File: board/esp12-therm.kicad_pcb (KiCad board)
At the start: 2 copper layers, 35.8 x 27.7 mm, 25 parts, among them J1 BATT, J2 I2C, J4 1W, Q1 PMF170XP, U1 TP4056_board, U2 ESP-12E, U3 TLV75533PDBV

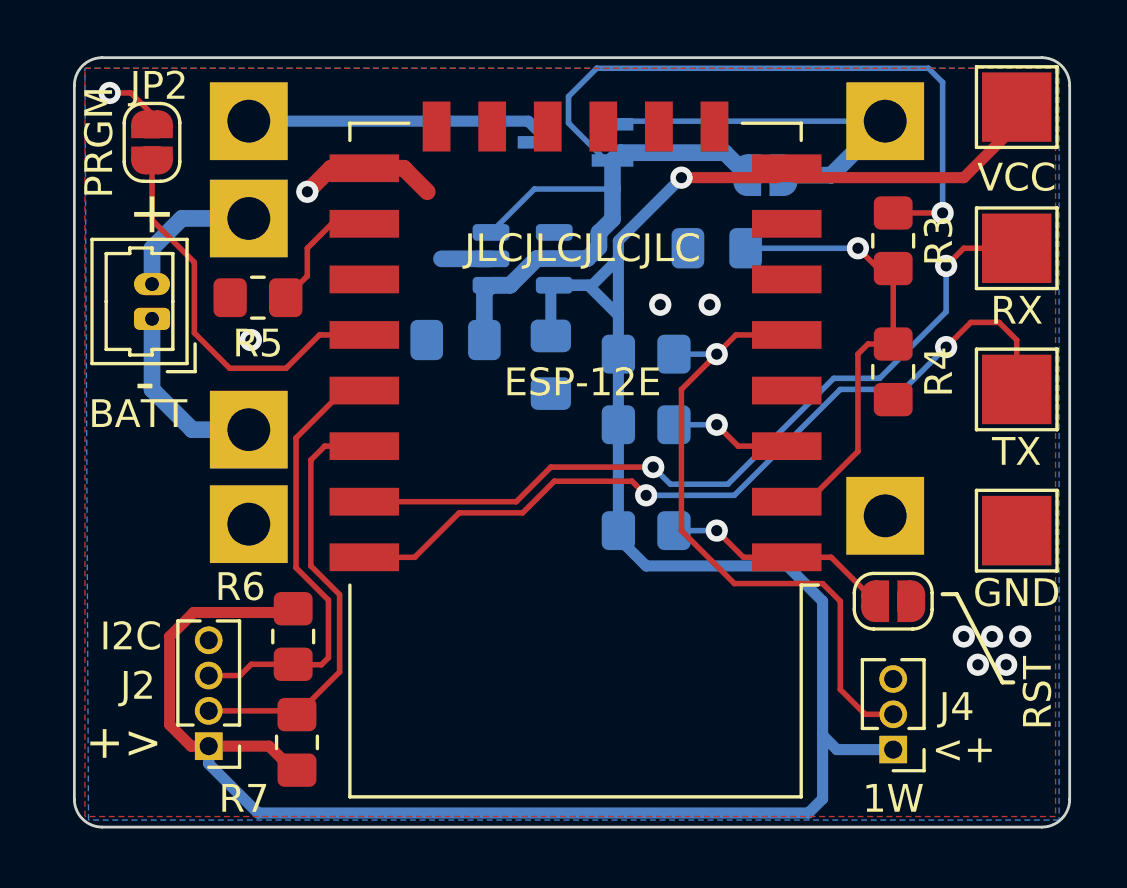
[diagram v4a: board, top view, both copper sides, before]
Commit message: Redesign to make it a fully breakout board: * Add pads for all pins * shrink board ad far as possible * place pull up resistors close to each other at the back * replace nmos with a schottky diode
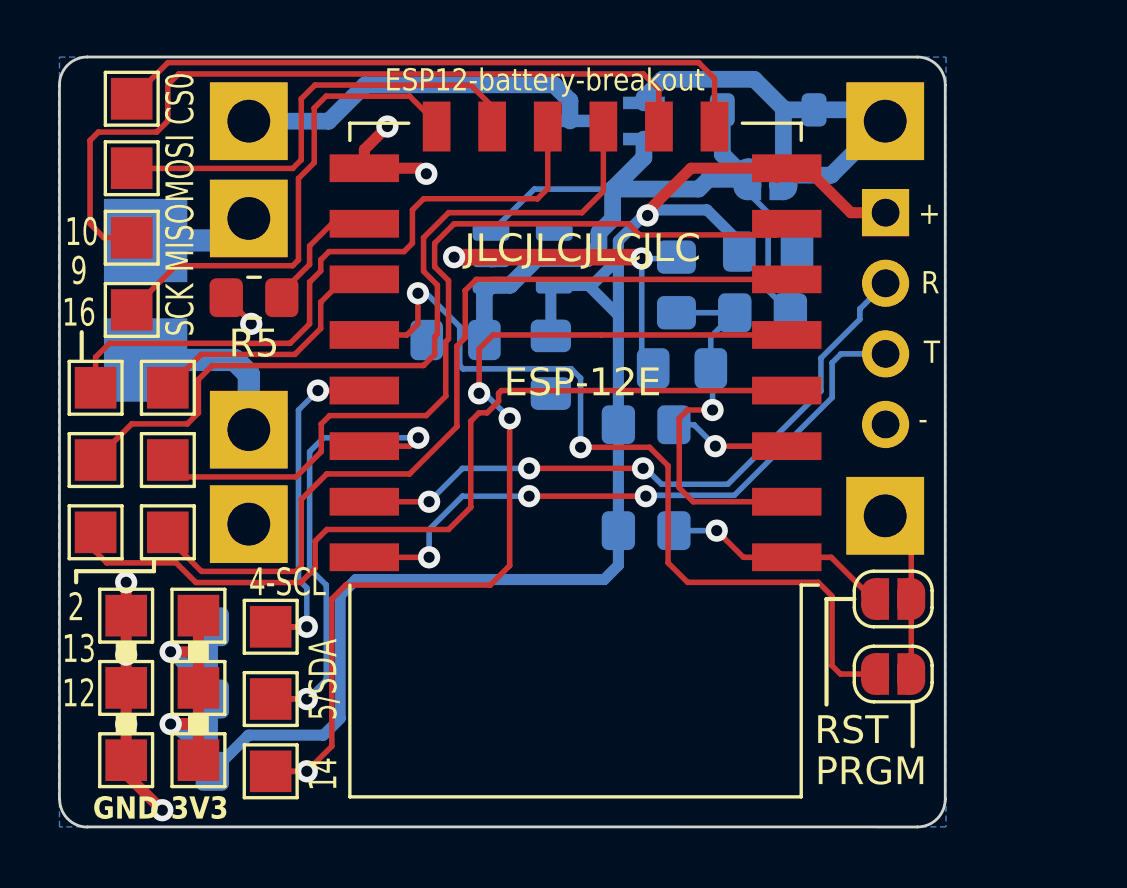
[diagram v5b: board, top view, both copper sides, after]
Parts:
- removed J4: 1W, Connector_PinHeader_1.27mm:PinHeader_1x03_P1.27mm_Vertical
- added C4: 100n, Capacitor_SMD:C_0805_2012Metric_Pad1.18x1.45mm_HandSolder, B.Cu at (122.5, 56.0)
- added D1: LL5817, Diode_SMD:D_SOD-123, B.Cu at (122.5, 50.9)
- added J3: DEBUG, Connector_PinSocket_2.54mm:PinSocket_1x04_P2.54mm_Vertical, F.Cu at (126.7, 54.6)
- added TP10: 10, TestPoint:TestPoint_Pad_1.5x1.5mm, F.Cu at (98.3, 60.9)
- added TP11: 4-SCL, TestPoint:TestPoint_Pad_1.5x1.5mm, F.Cu at (104.6, 69.5)
- added TP12: 2, TestPoint:TestPoint_Pad_1.5x1.5mm, F.Cu at (100.9, 60.9)
- added TP13: 3V3, TestPoint:TestPoint_Pad_1.5x1.5mm, F.Cu at (102.0, 71.7)
- added TP14: 3V3, TestPoint:TestPoint_Pad_1.5x1.5mm, F.Cu at (102.0, 74.3)
- added TP15: 3V3, TestPoint:TestPoint_Pad_1.5x1.5mm, F.Cu at (102.0, 69.1)
- added TP16: GND, TestPoint:TestPoint_Pad_1.5x1.5mm, F.Cu at (99.4, 69.1)
- added TP17: GND, TestPoint:TestPoint_Pad_1.5x1.5mm, F.Cu at (99.4, 74.3)
- added TP18: GND, TestPoint:TestPoint_Pad_1.5x1.5mm, F.Cu at (99.4, 71.7)
- added TP19: 14, TestPoint:TestPoint_Pad_1.5x1.5mm, F.Cu at (104.6, 74.7)
- added TP5: MISO, TestPoint:TestPoint_Pad_1.5x1.5mm, F.Cu at (99.6, 55.5)
- added TP6: MOSI, TestPoint:TestPoint_Pad_1.5x1.5mm, F.Cu at (99.6, 53.0)
- added TP7: SCK, TestPoint:TestPoint_Pad_1.5x1.5mm, F.Cu at (99.6, 58.1)
- added TP8: CS0, TestPoint:TestPoint_Pad_1.5x1.5mm, F.Cu at (99.6, 50.5)
- added TP9: 9, TestPoint:TestPoint_Pad_1.5x1.5mm, F.Cu at (98.3, 63.5)
- J1: value BATT -> B-; footprint Connector_Molex:Molex_PicoBlade_53047-0210_1x02_P1.25mm_Vertical -> TestPoint:TestPoint_Pad_3.0x3.0mm; moved to B.Cu
- J2: value I2C -> B+; footprint Connector_PinHeader_1.27mm:PinHeader_1x04_P1.27mm_Vertical -> TestPoint:TestPoint_Pad_3.0x3.0mm; moved to B.Cu
- R3, R6, R7: moved to B.Cu
- R4: value 470k -> 220k; moved to B.Cu
- TP1: value VCC -> 16; footprint TestPoint:TestPoint_Pad_2.5x2.5mm -> TestPoint:TestPoint_Pad_1.5x1.5mm
- TP2: value RX -> 13; footprint TestPoint:TestPoint_Pad_2.5x2.5mm -> TestPoint:TestPoint_Pad_1.5x1.5mm
- TP3: value TX -> 12; footprint TestPoint:TestPoint_Pad_2.5x2.5mm -> TestPoint:TestPoint_Pad_1.5x1.5mm
- TP4: value GND -> 5/SDA; footprint TestPoint:TestPoint_Pad_2.5x2.5mm -> TestPoint:TestPoint_Pad_1.5x1.5mm
- moved TP1 36.5 mm to (98.3, 66.1), turned to 0 degrees
- moved JP2 32.8 mm to (127.0, 71.2), turned to 180 degrees
- moved TP2 31.5 mm to (100.9, 63.5)
- moved TP3 31.0 mm to (100.9, 66.1)
- moved TP4 27.5 mm to (104.6, 72.1)
- moved R8 20.9 mm to (103.5, 74.7)
- moved J2 18.3 mm to (100.1, 55.6)
- moved R4 8.40 mm to (119.2, 57.2), turned to 90 degrees
- moved R3 5.37 mm to (122.3, 58.2), turned to 180 degrees
- moved C1 4.50 mm to (119.4, 60.2)
- moved R7 2.57 mm to (103.5, 72.1), turned to 0 degrees
- moved R6 1.94 mm to (103.5, 69.5), turned to 0 degrees
- moved J1 1.50 mm to (100.1, 59.9), turned to 180 degrees
- moved Q1 1.37 mm to (116.7, 51.3)
- moved JP3 0.15 mm to (122.4, 53.4)
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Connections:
- C3 pad 1: VCC -> +3V3
- J2 pad 1: VCC -> Net-(J2-Pin_1)
- R1 pad 1: VCC -> +3V3
- R2 pad 1: VCC -> +3V3
- R6 pad 1: VCC -> +3V3
- R7 pad 1: VCC -> +3V3
- R8 pad 1: VCC -> +3V3
- TP1 pad 1: VCC -> Net-(U2-GPIO16)
- TP2 pad 1: RXD -> Net-(U2-GPIO13)
- TP3 pad 1: TXD -> Net-(U2-GPIO12)
- TP4 pad 1: GND -> SDA
- U1 pad 5: Net-(J1-Pin_2) -> Net-(J2-Pin_1)
- U2 pad 10: unconnected-(U2-MISO-Pad10) -> Net-(U2-MISO)
- U2 pad 11: unconnected-(U2-GPIO9-Pad11) -> Net-(U2-GPIO9)
- U2 pad 12: unconnected-(U2-GPIO10-Pad12) -> Net-(U2-GPIO10)
- U2 pad 13: unconnected-(U2-MOSI-Pad13) -> Net-(U2-MOSI)
- U2 pad 14: unconnected-(U2-SCLK-Pad14) -> Net-(U2-SCLK)
- U2 pad 17: unconnected-(U2-GPIO2-Pad17) -> Net-(U2-GPIO2)
- U2 pad 4: unconnected-(U2-GPIO16-Pad4) -> Net-(U2-GPIO16)
- U2 pad 6: unconnected-(U2-GPIO12-Pad6) -> Net-(U2-GPIO12)
- U2 pad 7: unconnected-(U2-GPIO13-Pad7) -> Net-(U2-GPIO13)
- U2 pad 8: VCC -> +3V3
- U2 pad 9: unconnected-(U2-CS0-Pad9) -> Net-(U2-CS0)
- U3 pad 5: VCC -> +3V3
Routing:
- net VCC: track 90.3 -> 0.00 mm, vias 1 -> 0
- net +3V3: track 0.00 -> 74.1 mm, vias 0 -> 3
- net Net-(U2-GPIO16): track 0.00 -> 31.4 mm
- net Net-(U2-GPIO12): track 0.00 -> 31.4 mm
- net Net-(U2-GPIO13): track 0.00 -> 31.1 mm
- net Net-(U2-MISO): track 0.00 -> 28.5 mm
- net Net-(U2-GPIO9): track 0.00 -> 28.4 mm
- net GND: track 9.01 -> 33.1 mm, vias 10 -> 9
- net Net-(U2-GPIO10): track 0.00 -> 23.9 mm
- net Net-(U2-CS0): track 0.00 -> 23.5 mm
- net Net-(U2-SCLK): track 0.00 -> 17.6 mm
- net Net-(JP2-B): track 14.0 -> 31.1 mm, vias 0 -> 2
- net Net-(U2-MOSI): track 0.00 -> 16.5 mm
- net /VIN: track 43.4 -> 29.6 mm, vias 1 -> 0
- net 1W: track 23.4 -> 35.8 mm, vias 1 -> 3
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- removed copper zone on F.Cu, net GND
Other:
- board size 35.8 x 27.7 mm -> 31.9 x 27.7 mm
- board text added: "3V3"
- board text added: "ESP12-battery-breakout"
- board text added: "ESP12-battery-breakout (c) 2023 - Andreas Philipp https://gitlab.com/anphi/ esp12-battery-breakout"
- board text added: "GND"
- board text added: "PCB3D_BR_ESP12"
- board text added: "PCB3D_TL_ESP12"
- board text added: "R"
- board text added: "T"
- board text removed: "+>"
- board text removed: "<+"
- board text removed: "ESP12-thermometer (c) 2023"
- board text removed: "https://gitlab.com/anphi/esp12-thermometer"
